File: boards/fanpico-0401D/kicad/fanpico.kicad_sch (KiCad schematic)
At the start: 20 parts, among them Q2 BSS138, SW1 SW_Push, U1 SN74AHCT126, U4 Pico, U6 LM4040DBZ-3

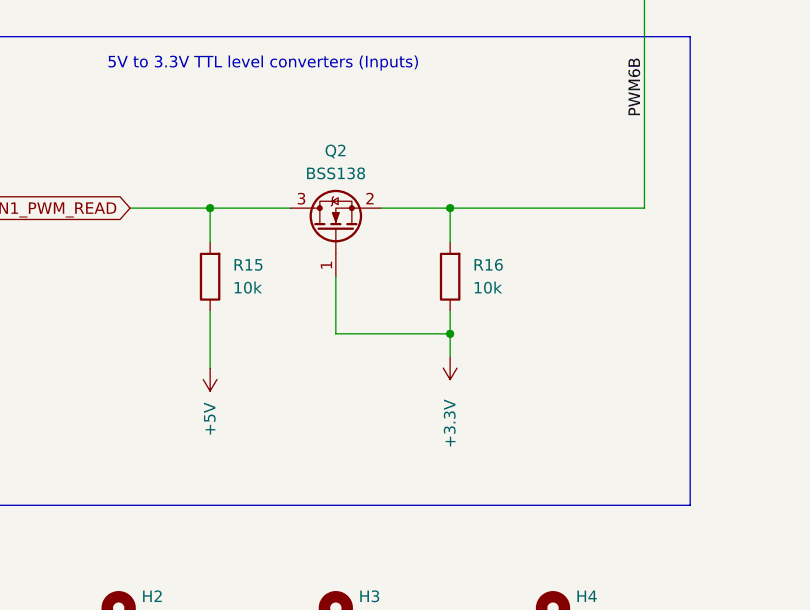
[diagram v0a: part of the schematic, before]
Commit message: Add new 0401D v1.1 PCB (#116)
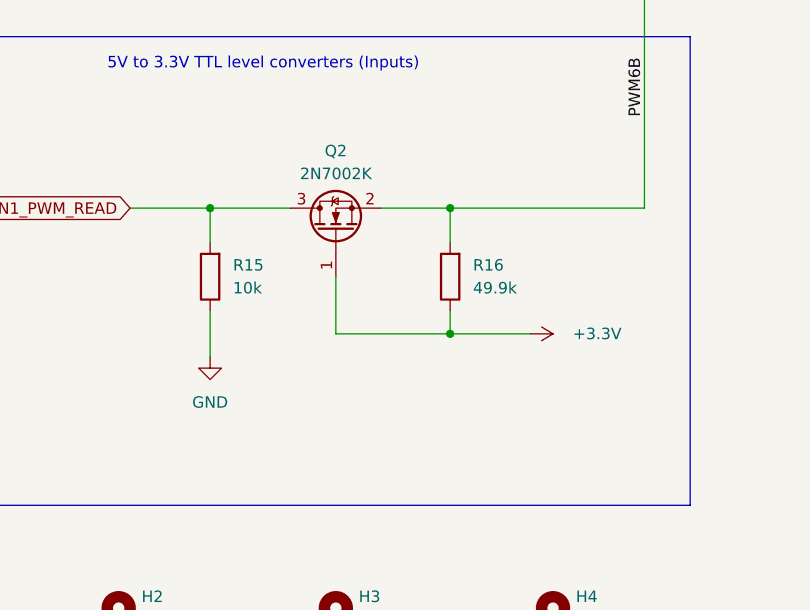
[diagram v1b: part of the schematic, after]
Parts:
- removed Q2: BSS138, Package_TO_SOT_SMD:SOT-23, symbol Transistor_FET:BSS138
- added Q2: 2N7002K, Package_TO_SOT_SMD:SOT-23, symbol Transistor_FET:2N7002K
- R16: value 10k -> 49.9k; LCSC Part Number C98220 -> C114624
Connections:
- net +3.3V: now also Q2.1 (G)
- net +5V: no longer R15.1
- net GND: now also R15.1
- net MBFAN1_PWM_READ: now also Q2.3 (D)
- net PWM6B: now also Q2.2 (S)
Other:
- title: FanPico-0401D v1.0 -> FanPico-0401D v1.1
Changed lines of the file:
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@@
 	(paper "A4")
 	(title_block
-		(title "FanPico-0401D v1.0")
-		(date "2024-07-22")
+		(title "FanPico-0401D v1.1")
+		(date "2024-08-15")
 		(company "Timo Kokkonen <tjko@iki.fi>")
 		(comment 3 "Fanpico firmware reference PCB.")
@@
 	(wire
 		(pts
-			(xy 59.69 152.4) (xy 59.69 158.75)
+			(xy 59.69 152.4) (xy 59.69 157.48)
 		)
 		(stroke
@@
 	(wire
 		(pts
+			(xy 95.25 154.94) (xy 86.36 154.94)
+		)
+		(stroke
+			(width 0)
+			(type default)
+		)
+	)
+	(wire
+		(pts
 			(xy 256.54 144.78) (xy 256.54 142.24)
 		)
@@
 	(wire
 		(pts
-			(xy 86.36 154.94) (xy 86.36 157.48)
-		)
-		(stroke
-			(width 0)
-			(type default)
-		)
-	)
-	(wire
-		(pts
 			(xy 36.83 26.67) (xy 26.67 26.67)
 		)
@@
 	)
 	(symbol
-		(lib_id "Transistor_FET:BSS138")
-		(at 73.66 143.51 90)
-		(unit 1)
-		(exclude_from_sim no)
-		(in_bom yes)
-		(on_board yes)
-		(dnp no)
-		(fields_autoplaced yes)
-		(property "Reference" "Q2"
-			(at 73.66 134.62 90)
-			(effects
-				(font
-					(size 1.27 1.27)
-				)
-			)
-		)
-		(property "Value" "BSS138"
-			(at 73.66 137.16 90)
-			(effects
-				(font
-					(size 1.27 1.27)
-				)
-			)
-		)
-		(property "Footprint" "Package_TO_SOT_SMD:SOT-23"
-			(at 75.565 138.43 0)
-			(effects
-				(font
-					(size 1.27 1.27)
-					(italic yes)
-				)
-				(justify left)
-				(hide yes)
-			)
-		)
-		(property "Datasheet" "https://www.onsemi.com/pub/Collateral/BSS138-D.PDF"
-			(at 77.47 138.43 0)
-			(effects
-				(font
-					(size 1.27 1.27)
-				)
-				(justify left)
-				(hide yes)
-			)
-		)
-		(property "Description" "50V Vds, 0.22A Id, N-Channel MOSFET, SOT-23"
-			(at 73.66 143.51 0)
-			(effects
-				(font
-					(size 1.27 1.27)
-				)
-				(hide yes)
-			)
-		)
-		(property "LCSC Part Number" "C82045 or C427380"
-			(at 73.66 143.51 90)
-			(effects
-				(font
-					(size 1.27 1.27)
-				)
-				(hide yes)
-			)
-		)
-		(property "JCLC Part Number" ""
-			(at 73.66 143.51 0)
-			(effects
-				(font
-					(size 1.27 1.27)
-				)
-				(hide yes)
-			)
-		)
-		(property "Mouser Part Number" ""
-			(at 73.66 143.51 0)
-			(effects
-				(font
-					(size 1.27 1.27)
-				)
-				(hide yes)
-			)
-		)
-		(pin "3"
-		)
-		(pin "2"
-		)
-		(pin "1"
-		)
-		(instances
-			(project ""
-				(path "/e63e39d7-6ac0-4ffd-8aa3-1841a4541b55"
-					(reference "Q2")
-					(unit 1)
-				)
-			)
-		)
-	)
-	(symbol
 		(lib_id "Reference_Voltage:LM4040DBZ-3")
 		(at 256.54 138.43 90)
@@
 	)
 	(symbol
+		(lib_id "power:GND")
+		(at 59.69 157.48 0)
+		(unit 1)
+		(exclude_from_sim no)
+		(in_bom yes)
+		(on_board yes)
+		(dnp no)
+		(fields_autoplaced yes)
+		(property "Reference" "#PWR012"
+			(at 59.69 163.83 0)
+			(effects
+				(font
+					(size 1.27 1.27)
+				)
+				(hide yes)
+			)
+		)
+		(property "Value" "GND"
+			(at 59.69 162.56 0)
+			(effects
+				(font
+					(size 1.27 1.27)
+				)
+			)
+		)
+		(property "Footprint" ""
+			(at 59.69 157.48 0)
+			(effects
+				(font
+					(size 1.27 1.27)
+				)
+				(hide yes)
+			)
+		)
+		(property "Datasheet" ""
+			(at 59.69 157.48 0)
+			(effects
+				(font
+					(size 1.27 1.27)
+				)
+				(hide yes)
+			)
+		)
+		(property "Description" "Power symbol creates a global label with name \"GND\" , ground"
+			(at 59.69 157.48 0)
+			(effects
+				(font
+					(size 1.27 1.27)
+				)
+				(hide yes)
+			)
+		)
+		(pin "1"
+		)
+		(instances
+			(project "fanpico"
+				(path "/e63e39d7-6ac0-4ffd-8aa3-1841a4541b55"
+					(reference "#PWR012")
+					(unit 1)
+				)
+			)
+		)
+	)
+	(symbol
 		(lib_id "Device:R")
 		(at 36.83 34.29 180)
@@
 			)
 		)
-		(property "Value" "10k"
+		(property "Value" "49.9k"
 			(at 88.9 149.8599 0)
 			(effects
@@
 			)
 		)
-		(property "LCSC Part Number" "C98220"
+		(property "LCSC Part Number" "C114624"
 			(at 86.36 148.59 0)
 			(effects
@@
 	)
 	(symbol
-		(lib_id "power:+5V")
-		(at 59.69 158.75 180)
-		(unit 1)
-		(exclude_from_sim no)
-		(in_bom yes)
-		(on_board yes)
-		(dnp no)
-		(property "Reference" "#PWR06"
-			(at 59.69 154.94 0)
-			(effects
-				(font
-					(size 1.27 1.27)
-				)
-				(hide yes)
-			)
-		)
-		(property "Value" "+5V"
-			(at 59.69 162.56 90)
-			(effects
-				(font
-					(size 1.27 1.27)
-				)
-				(justify left)
-			)
-		)
-		(property "Footprint" ""
-			(at 59.69 158.75 0)
-			(effects
-				(font
-					(size 1.27 1.27)
-				)
-				(hide yes)
-			)
-		)
-		(property "Datasheet" ""
-			(at 59.69 158.75 0)
-			(effects
-				(font
-					(size 1.27 1.27)
-				)
-				(hide yes)
-			)
-		)
-		(property "Description" "Power symbol creates a global label with name \"+5V\""
-			(at 59.69 158.75 0)
-			(effects
-				(font
-					(size 1.27 1.27)
-				)
-				(hide yes)
-			)
-		)
-		(pin "1"
-		)
-		(instances
-			(project "fanpico"
-				(path "/e63e39d7-6ac0-4ffd-8aa3-1841a4541b55"
-					(reference "#PWR06")
-					(unit 1)
-				)
-			)
-		)
-	)
-	(symbol
 		(lib_id "Device:C_Small")
 		(at 236.22 138.43 0)
@@
 	)
 	(symbol
+		(lib_id "Transistor_FET:2N7002K")
+		(at 73.66 143.51 90)
+		(unit 1)
+		(exclude_from_sim no)
+		(in_bom yes)
+		(on_board yes)
+		(dnp no)
+		(fields_autoplaced yes)
+		(property "Reference" "Q2"
+			(at 73.66 134.62 90)
+			(effects
+				(font
+					(size 1.27 1.27)
+				)
+			)
+		)
+		(property "Value" "2N7002K"
+			(at 73.66 137.16 90)
+			(effects
+				(font
+					(size 1.27 1.27)
+				)
+			)
+		)
+		(property "Footprint" "Package_TO_SOT_SMD:SOT-23"
+			(at 75.565 138.43 0)
+			(effects
+				(font
+					(size 1.27 1.27)
+					(italic yes)
+				)
+				(justify left)
+				(hide yes)
+			)
+		)
+		(property "Datasheet" "https://www.diodes.com/assets/Datasheets/2N7002K.pdf"
+			(at 73.66 143.51 0)
+			(effects
+				(font
+					(size 1.27 1.27)
+				)
+				(justify left)
+				(hide yes)
+			)
+		)
+		(property "Description" "0.38A Id, 60V Vds, N-Channel MOSFET, SOT-23"
+			(at 73.66 143.51 0)
+			(effects
+				(font
+					(size 1.27 1.27)
+				)
+				(hide yes)
+			)
+		)
+		(property "LCSC Part Number" "C85047"
+			(at 73.66 143.51 0)
+			(effects
+				(font
+					(size 1.27 1.27)
+				)
+				(hide yes)
+			)
+		)
+		(property "JCLC Part Number" ""
+			(at 73.66 143.51 0)
+			(effects
+				(font
+					(size 1.27 1.27)
+				)
+				(hide yes)
+			)
+		)
+		(property "Mouser Part Number" "512-2N7002K"
+			(at 73.66 143.51 0)
+			(effects
+				(font
+					(size 1.27 1.27)
+				)
+				(hide yes)
+			)
+		)
+		(pin "1"
+		)
+		(pin "2"
+		)
+		(pin "3"
+		)
+		(instances
+			(project "fanpico"
+				(path "/e63e39d7-6ac0-4ffd-8aa3-1841a4541b55"
+					(reference "Q2")
+					(unit 1)
+				)
+			)
+		)
+	)
+	(symbol
 		(lib_id "Mechanical:MountingHole_Pad")
 		(at 25.4 186.69 0)
@@
 	(symbol
 		(lib_id "power:+3.3V")
-		(at 86.36 157.48 180)
+		(at 95.25 154.94 270)
 		(unit 1)
 		(exclude_from_sim no)
@@
 		(dnp no)
 		(property "Reference" "#PWR04"
-			(at 86.36 153.67 0)
+			(at 91.44 154.94 0)
 			(effects
 				(font
@@
 		)
 		(property "Value" "+3.3V"
-			(at 86.36 167.64 90)
+			(at 105.41 154.94 90)
 			(effects
 				(font
@@
 		)
 		(property "Footprint" ""
-			(at 86.36 157.48 0)
+			(at 95.25 154.94 0)
 			(effects
 				(font
@@
 		)
 		(property "Datasheet" ""
-			(at 86.36 157.48 0)
+			(at 95.25 154.94 0)
 			(effects
 				(font
@@
 		)
 		(property "Description" "Power symbol creates a global label with name \"+3.3V\""
-			(at 86.36 157.48 0)
+			(at 95.25 154.94 0)
 			(effects
 				(font
